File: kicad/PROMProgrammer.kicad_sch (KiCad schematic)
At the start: 28 parts, among them J1 Control / Program Select Swit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, J2 USB_C_Receptacle_PowerOnly_6P, J3 Conn_01x02, J4 USB_A, J5 Barrel_Jack, SW8 SW_SPDT, U1 74S188, U2 MC34063AP

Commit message: Starting docs
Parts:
- D10: footprint Diode_THT:D_DO-41_SOD81_P12.70mm_Horizontal -> Diode_THT:D_DO-41_SOD81_P10.16mm_Horizontal
- U1: footprint AAA_Project:DIP-16_W7.62mm_wide_TPH -> Package_DIP:DIP-16_W7.62mm
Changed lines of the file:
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@@
 (kicad_sch
-	(version 20231120)
+	(version 20250114)
 	(generator "eeschema")
-	(generator_version "8.0")
+	(generator_version "9.0")
 	(paper "A3")
 	(title_block
 		(title "PROM Programmer")
-		(date "2024-11-17")
-		(rev "V1.1")
+		(date "2025-03-27")
+		(rev "V1.4")
+	)
+	(text "Vin 		5V\nVout 		16V\nIout 		155mA\nVripple 	63mV(pp)\nFmin 		50kHz"
+		(exclude_from_sim no)
+		(at 59.944 193.548 0)
+		(effects
+			(font
+				(size 1.27 1.27)
+			)
+			(justify left)
+		)
+	)
+	(text "Switch pin groups: E.g. 1,2,3 - Pin 2 is common"
+		(exclude_from_sim no)
+		(at 319.278 168.402 0)
+		(effects
+			(font
+				(size 1.27 1.27)
+			)
+		)
+	)
+	(text "Ct=592 pF\nIpk=1193 mA\nRsc=0.251 Ohm\nLmin=50 uH\nCo=328 uF\nR=180 Ohm\nR1=1.1k R2=13k (16.02V)"
+		(exclude_from_sim no)
+		(at 60.198 211.074 0)
+		(effects
+			(font
+				(size 1.27 1.27)
+			)
+			(justify left)
+		)
+	)
+	(text "KUSBX-AS1N"
+		(exclude_from_sim no)
+		(at 281.432 69.088 0)
+		(effects
+			(font
+				(size 1.27 1.27)
+			)
+		)
+	)
+	(text "2MS1T2B3M2QES"
+		(exclude_from_sim no)
+		(at 368.808 74.168 0)
+		(effects
+			(font
+				(size 1.27 1.27)
+			)
+		)
+	)
+	(text "16v Supply"
+		(exclude_from_sim no)
+		(at 110.49 132.588 0)
+		(effects
+			(font
+				(size 2.54 2.54)
+				(thickness 0.508)
+				(bold yes)
+			)
+		)
+	)
+	(text "PBH4UEENAGX - ON - ON"
+		(exclude_from_sim no)
+		(at 319.786 160.274 0)
+		(effects
+			(font
+				(size 1.27 1.27)
+			)
+		)
+	)
+	(text "WURTH ELEKTRONIK\n694108301002\n\n"
+		(exclude_from_sim no)
+		(at 349.758 107.95 0)
+		(effects
+			(font
+				(size 1.27 1.27)
+			)
+		)
+	)
+	(text "USB4125-GF-A\n"
+		(exclude_from_sim no)
+		(at 302.006 105.664 0)
+		(effects
+			(font
+				(size 1.27 1.27)
+			)
+		)
+	)
+	(text "Amphenol_12401548E4"
+		(exclude_from_sim no)
+		(at 230.886 81.28 0)
+		(effects
+			(font
+				(size 1.27 1.27)
+			)
+		)
 	)
 	(junction
@@
 		)
 	)
-	(text "Vin 		5V\nVout 		16V\nIout 		155mA\nVripple 	63mV(pp)\nFmin 		50kHz"
-		(exclude_from_sim no)
-		(at 59.944 193.548 0)
-		(effects
-			(font
-				(size 1.27 1.27)
-			)
-			(justify left)
-		)
-	)
-	(text "Switch pin groups: E.g. 1,2,3 - Pin 2 is common"
-		(exclude_from_sim no)
-		(at 319.278 168.402 0)
-		(effects
-			(font
-				(size 1.27 1.27)
-			)
-		)
-	)
-	(text "Ct=592 pF\nIpk=1193 mA\nRsc=0.251 Ohm\nLmin=50 uH\nCo=328 uF\nR=180 Ohm\nR1=1.1k R2=13k (16.02V)"
-		(exclude_from_sim no)
-		(at 60.198 211.074 0)
-		(effects
-			(font
-				(size 1.27 1.27)
-			)
-			(justify left)
-		)
-	)
-	(text "KUSBX-AS1N"
-		(exclude_from_sim no)
-		(at 281.432 69.088 0)
-		(effects
-			(font
-				(size 1.27 1.27)
-			)
-		)
-	)
-	(text "2MS1T2B3M2QES"
-		(exclude_from_sim no)
-		(at 368.808 74.168 0)
-		(effects
-			(font
-				(size 1.27 1.27)
-			)
-		)
-	)
-	(text "16v Supply"
-		(exclude_from_sim no)
-		(at 110.49 132.588 0)
-		(effects
-			(font
-				(size 2.54 2.54)
-				(thickness 0.508)
-				(bold yes)
-			)
-		)
-	)
-	(text "PBH4UEENAGX - ON - ON"
-		(exclude_from_sim no)
-		(at 319.786 160.274 0)
-		(effects
-			(font
-				(size 1.27 1.27)
-			)
-		)
-	)
-	(text "WURTH ELEKTRONIK\n694108301002\n\n"
-		(exclude_from_sim no)
-		(at 349.758 107.95 0)
-		(effects
-			(font
-				(size 1.27 1.27)
-			)
-		)
-	)
-	(text "USB4125-GF-A\n"
-		(exclude_from_sim no)
-		(at 302.006 105.664 0)
-		(effects
-			(font
-				(size 1.27 1.27)
-			)
-		)
-	)
-	(text "Amphenol_12401548E4"
-		(exclude_from_sim no)
-		(at 230.886 81.28 0)
-		(effects
-			(font
-				(size 1.27 1.27)
-			)
-		)
-	)
 	(global_label "B7"
 		(shape input)
@@
 			)
 		)
-		(property "Footprint" "AAA_Project:DIP-16_W7.62mm_wide_TPH"
+		(property "Footprint" "Package_DIP:DIP-16_W7.62mm"
 			(at 204.47 202.438 0)
 			(effects
@@
 			)
 		)
-		(property "Footprint" "Diode_THT:D_DO-41_SOD81_P12.70mm_Horizontal"
+		(property "Footprint" "Diode_THT:D_DO-41_SOD81_P10.16mm_Horizontal"
 			(at 131.445 181.61 0)
 			(effects
@@
 		(at 165.1 38.1)
 		(size 25.4 24.13)
+		(exclude_from_sim no)
+		(in_bom yes)
+		(on_board yes)
+		(dnp no)
 		(fields_autoplaced yes)
 		(stroke
@@
 		(at 215.9 38.1)
 		(size 25.4 25.4)
+		(exclude_from_sim no)
+		(in_bom yes)
+		(on_board yes)
+		(dnp no)
 		(fields_autoplaced yes)
 		(stroke
@@
 		)
 	)
+	(embedded_fonts no)
 )

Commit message: Minor layout changes
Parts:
- added TP7: GND, TestPoint:TestPoint_THTPad_2.0x2.0mm_Drill1.0mm, symbol Connector:TestPoint
- U1: footprint Package_DIP:DIP-16_W7.62mm -> Socket:DIP_Socket-16_W4.3_W5.08_W7.62_W10.16_W10.9_3M_216-3340-00-0602J
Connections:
- net GND: now also TP7.1
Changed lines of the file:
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@@
 	(title_block
 		(title "PROM Programmer")
-		(date "2025-04-06")
-		(rev "V1.4")
+		(date "2025-05-24")
+		(rev "2.0")
 	)
 	(text "Vin 		5V\nVout 		16V\nIout 		155mA\nVripple 	63mV(pp)\nFmin 		50kHz"
@@
 	)
 	(junction
+		(at 101.6 205.74)
+		(diameter 0)
+		(color 0 0 0 0)
+	)
+	(junction
 		(at 322.58 97.79)
 		(diameter 0)
@@
 	(wire
 		(pts
+			(xy 101.6 205.74) (xy 113.03 205.74)
+		)
+		(stroke
+			(width 0)
+			(type default)
+		)
+	)
+	(wire
+		(pts
 			(xy 322.58 67.31) (xy 322.58 97.79)
 		)
@@
 	(wire
 		(pts
+			(xy 101.6 205.74) (xy 101.6 210.82)
+		)
+		(stroke
+			(width 0)
+			(type default)
+		)
+	)
+	(wire
+		(pts
 			(xy 50.8 29.21) (xy 50.8 27.94)
 		)
@@
 	(wire
 		(pts
-			(xy 101.6 198.12) (xy 101.6 203.2)
+			(xy 101.6 198.12) (xy 101.6 205.74)
 		)
 		(stroke
@@
 	(symbol
 		(lib_id "power:GND")
-		(at 101.6 203.2 0)
+		(at 101.6 210.82 0)
 		(unit 1)
 		(exclude_from_sim no)
@@
 		(fields_autoplaced yes)
 		(property "Reference" "#PWR010"
-			(at 101.6 209.55 0)
+			(at 101.6 217.17 0)
 			(effects
 				(font
@@
 		)
 		(property "Value" "GND"
-			(at 101.6 208.28 0)
+			(at 101.6 215.9 0)
 			(effects
 				(font
@@
 		)
 		(property "Footprint" ""
-			(at 101.6 203.2 0)
+			(at 101.6 210.82 0)
 			(effects
 				(font
@@
 		)
 		(property "Datasheet" ""
-			(at 101.6 203.2 0)
+			(at 101.6 210.82 0)
 			(effects
 				(font
@@
 		)
 		(property "Description" "Power symbol creates a global label with name \"GND\" , ground"
-			(at 101.6 203.2 0)
+			(at 101.6 210.82 0)
 			(effects
 				(font
@@
 	)
 	(symbol
+		(lib_id "Connector:TestPoint")
+		(at 113.03 205.74 0)
+		(unit 1)
+		(exclude_from_sim no)
+		(in_bom yes)
+		(on_board yes)
+		(dnp no)
+		(fields_autoplaced yes)
+		(property "Reference" "TP7"
+			(at 115.57 201.1679 0)
+			(effects
+				(font
+					(size 1.27 1.27)
+				)
+				(justify left)
+			)
+		)
+		(property "Value" "GND"
+			(at 115.57 203.7079 0)
+			(effects
+				(font
+					(size 1.27 1.27)
+				)
+				(justify left)
+			)
+		)
+		(property "Footprint" "TestPoint:TestPoint_THTPad_2.0x2.0mm_Drill1.0mm"
+			(at 118.11 205.74 0)
+			(effects
+				(font
+					(size 1.27 1.27)
+				)
+				(hide yes)
+			)
+		)
+		(property "Datasheet" "~"
+			(at 118.11 205.74 0)
+			(effects
+				(font
+					(size 1.27 1.27)
+				)
+				(hide yes)
+			)
+		)
+		(property "Description" "test point"
+			(at 113.03 205.74 0)
+			(effects
+				(font
+					(size 1.27 1.27)
+				)
+				(hide yes)
+			)
+		)
+		(pin "1"
+		)
+		(instances
+			(project "PROMProgrammer"
+				(path "/aea5f780-7057-4d23-a657-1d11de8949a0"
+					(reference "TP7")
+					(unit 1)
+				)
+			)
+		)
+	)
+	(symbol
 		(lib_id "power:GND")
 		(at 127 203.2 0)
@@
 			)
 		)
-		(property "Footprint" "Package_DIP:DIP-16_W7.62mm"
+		(property "Footprint" "Socket:DIP_Socket-16_W4.3_W5.08_W7.62_W10.16_W10.9_3M_216-3340-00-0602J"
 			(at 204.47 202.438 0)
 			(effects

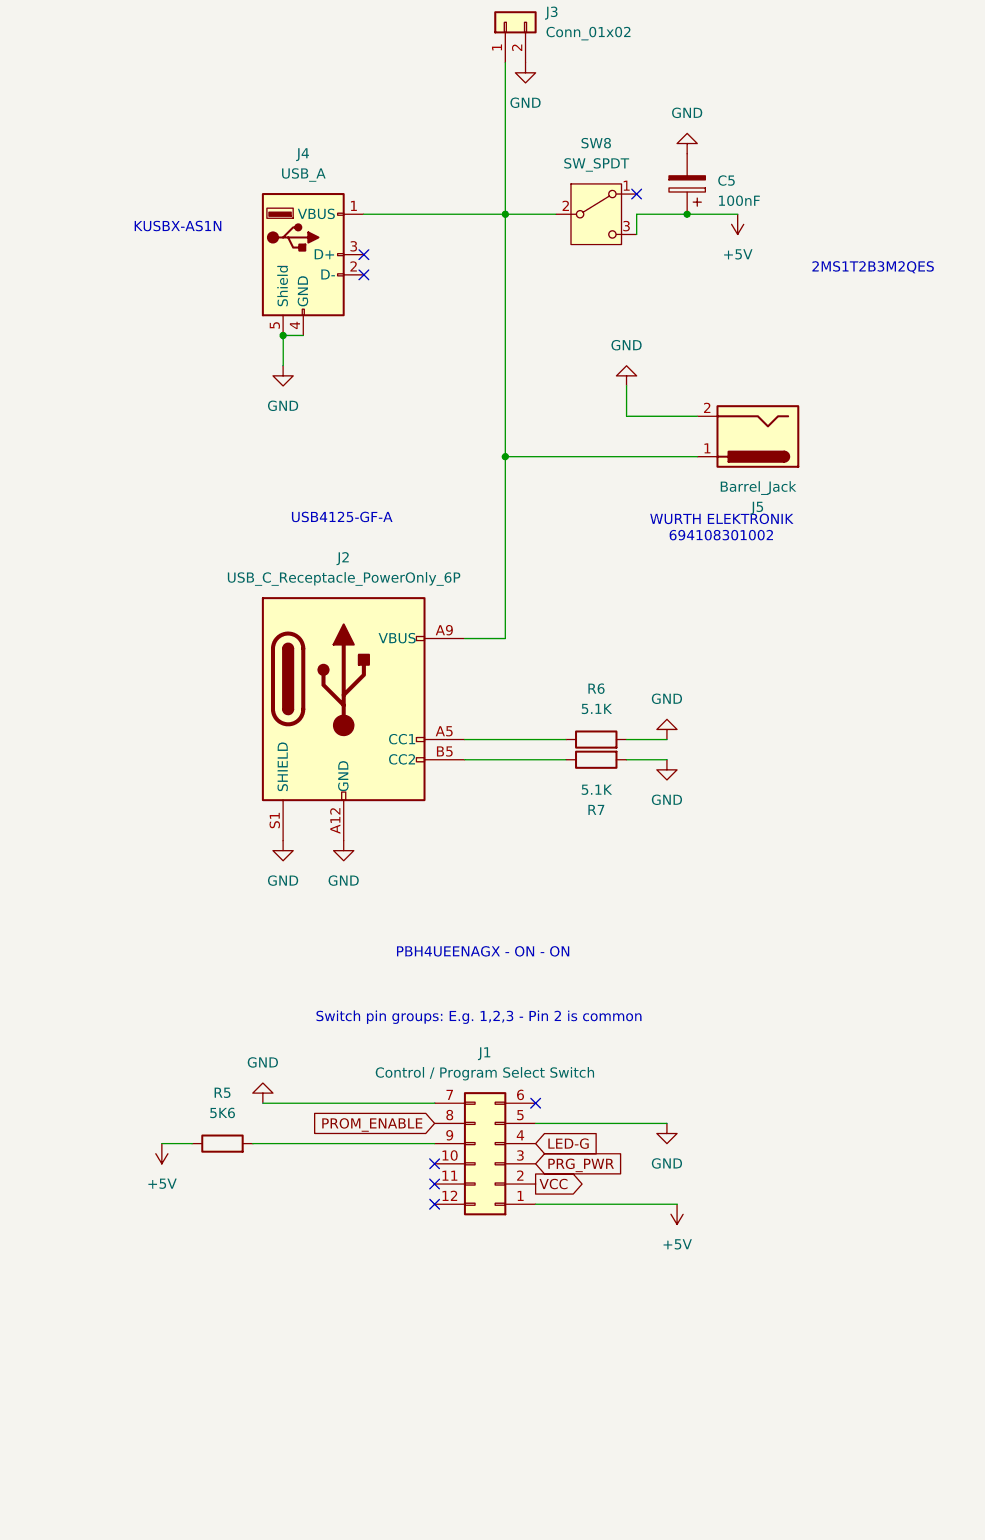
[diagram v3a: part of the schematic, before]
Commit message: Update transistors
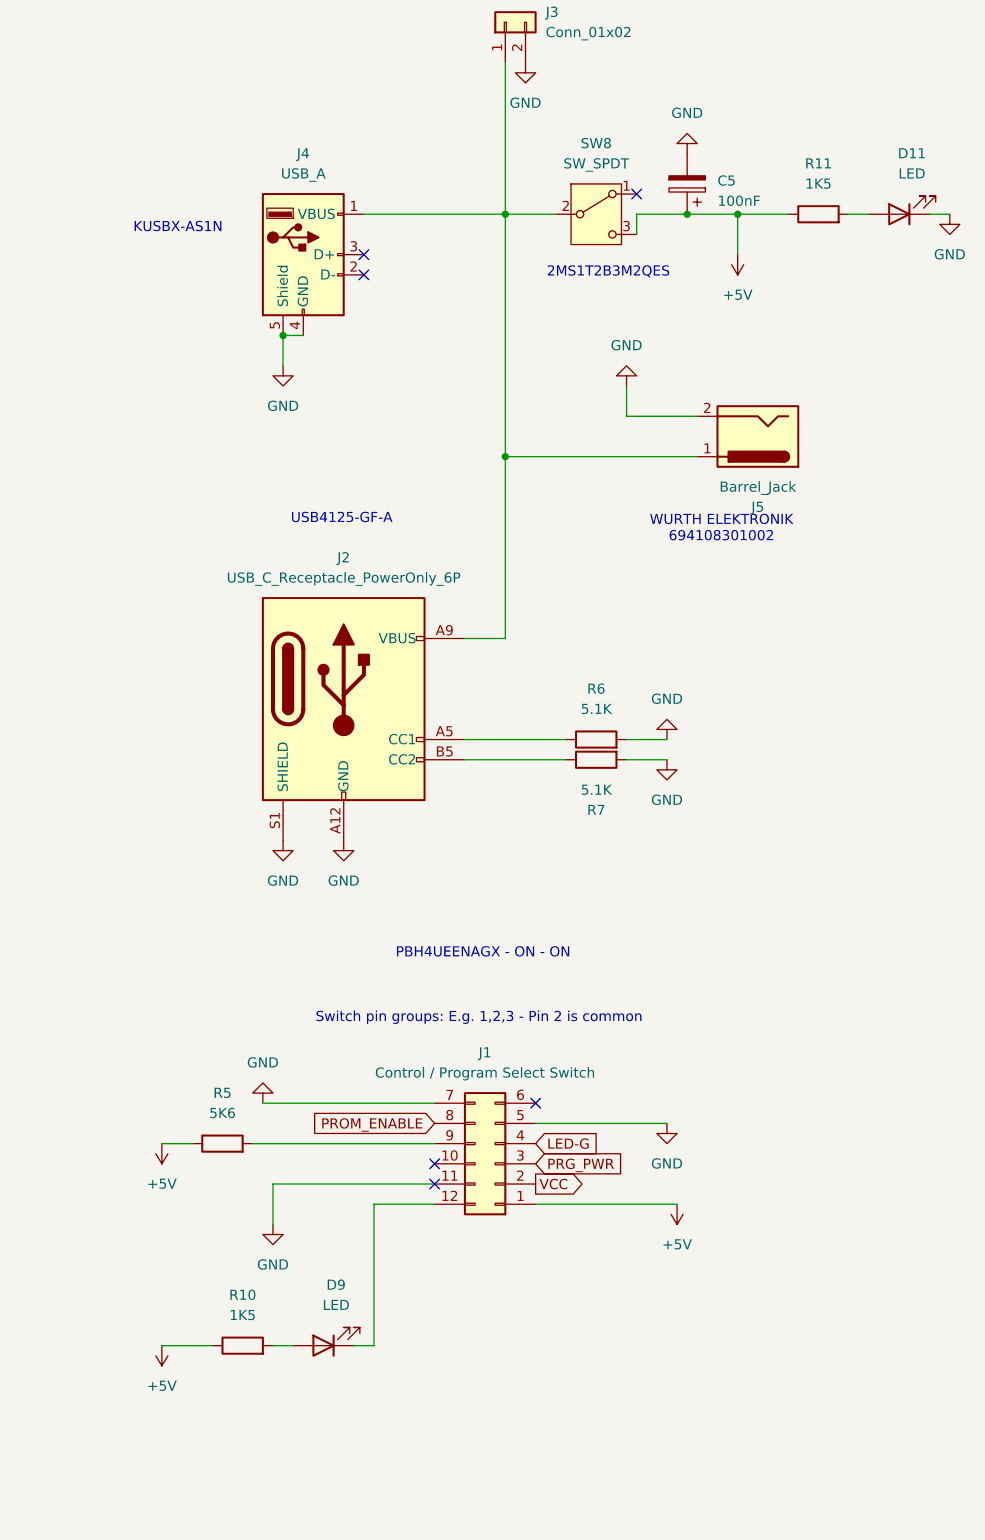
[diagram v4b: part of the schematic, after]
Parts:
- added D11, D9: LED, LED_THT:LED_D3.0mm, symbol Device:LED
- added R10, R11: 1K5, Resistor_THT:R_Axial_DIN0309_L9.0mm_D3.2mm_P12.70mm_Horizontal, symbol Device:R
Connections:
- net +5V: now also R10.1, R11.1
- net GND: now also J1.11 (Pin_11), D11.1 (K)
- net at J1.12 (Pin_12): now also D9.1 (K)
- new net: D11.2 (A), R11.2
- new net: D9.2 (A), R10.2
- no-connect marks 7 -> 6

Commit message: All working and tidy
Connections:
- no-connect marks 6 -> 5
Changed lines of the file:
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@@
 	(title_block
 		(title "PROM Programmer")
-		(date "2025-05-24")
-		(rev "2.0")
+		(date "2025-08-22")
+		(rev "3.1 ")
 	)
 	(text "Vin 		5V\nVout 		16V\nIout 		155mA\nVripple 	63mV(pp)\nFmin 		50kHz"
@@
 	)
 	(no_connect
-		(at 313.69 189.23)
-	)
-	(no_connect
